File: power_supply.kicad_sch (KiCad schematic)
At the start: 24 parts, among them U3 ST1S10PHR, U4 ST1S09IPUR

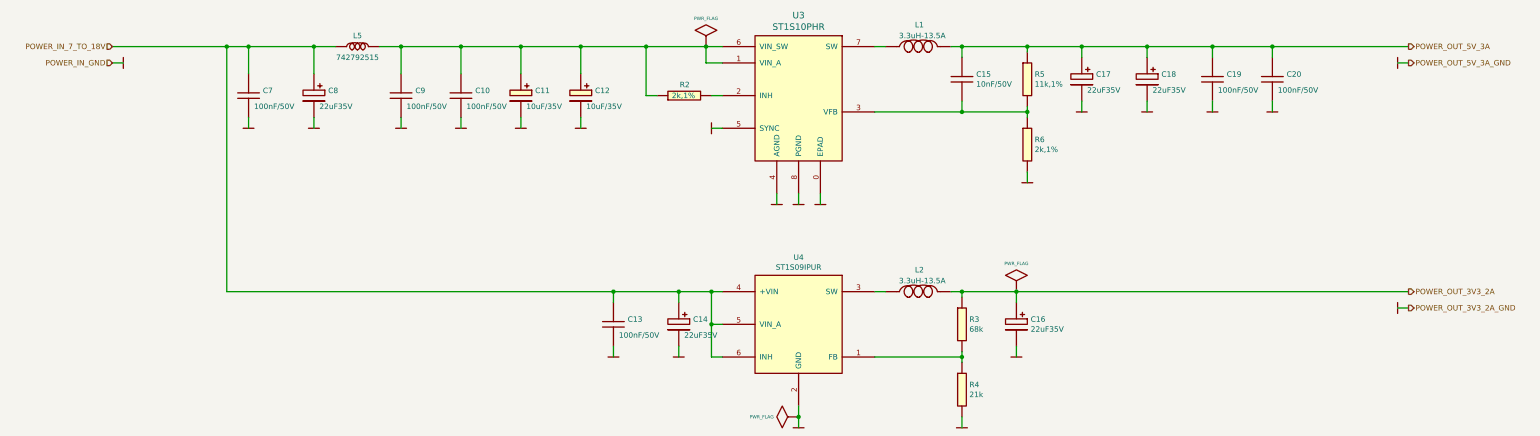
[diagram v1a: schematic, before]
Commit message: Reworked schematic and applied changes on pcb related with mini pci express
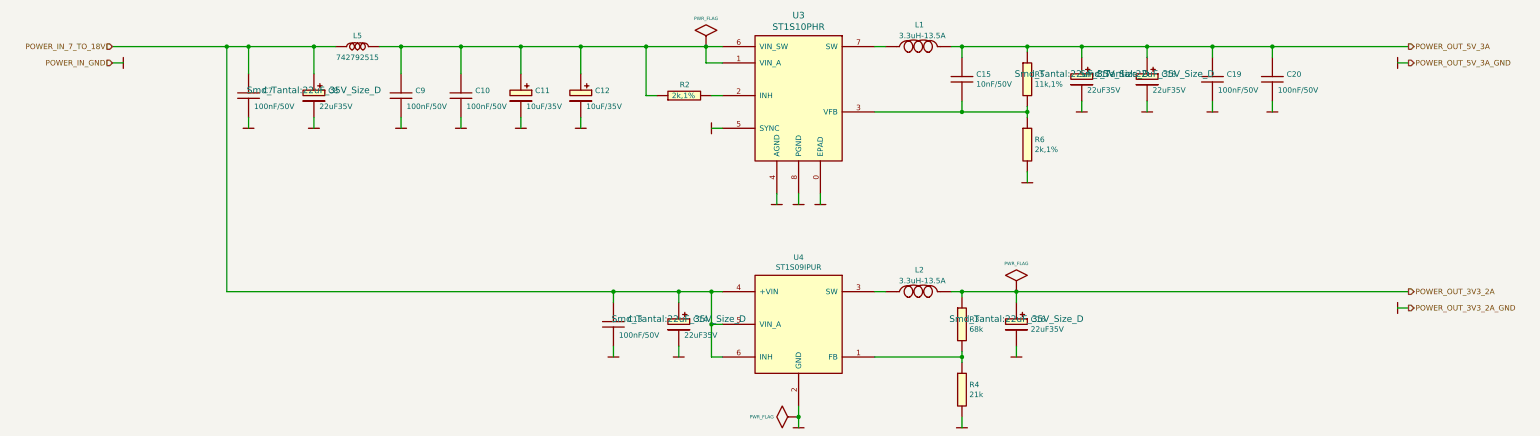
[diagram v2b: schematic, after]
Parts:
- C10, C13, C19, C20, C7, C9: symbol Capacitors_Smd0603:100nF_0603 -> Capacitors_Smd0603:100n
- C14, C16, C17, C18, C8: symbol Capacitors_Smd_Tantal:22uF35V -> Capacitors_Smd_Tantal:22uF_35V
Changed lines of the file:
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@@
     (pin "2")
   )
-  (symbol (lib_id "Capacitors_Smd0603:100nF_0603") (at 85.09 114.3 0) (unit 1)
+  (symbol (lib_id "Capacitors_Smd0603:100n") (at 85.09 114.3 0) (unit 1)
     (in_bom yes) (on_board yes)
     (property "Reference" "C7" (id 0) (at 88.4174 113.1316 0)
@@
     (pin "2")
   )
-  (symbol (lib_id "Capacitors_Smd_Tantal:22uF35V") (at 100.33 113.03 0) (unit 1)
+  (symbol (lib_id "Capacitors_Smd_Tantal:22uF_35V") (at 100.33 113.03 0) (unit 1)
     (in_bom yes) (on_board yes)
     (property "Reference" "C8" (id 0) (at 103.6574 113.1316 0)
@@
     )
     (property "Footprint" "Smd_Tantal:22uF_35V_Size_D" (id 2) (at 100.33 113.03 0)
-      (effects (font (size 1.524 1.524)) hide)
+      (effects (font (size 1.524 1.524)))
     )
     (property "Datasheet" "https://www.tme.eu/Document/a5d90d85079967994fb49c0e8f8ad6e9/293d.pdf" (id 3) (at 100.33 113.03 0)
@@
     (pin "2")
   )
-  (symbol (lib_id "Capacitors_Smd0603:100nF_0603") (at 120.65 114.3 0) (unit 1)
+  (symbol (lib_id "Capacitors_Smd0603:100n") (at 120.65 114.3 0) (unit 1)
     (in_bom yes) (on_board yes)
     (property "Reference" "C9" (id 0) (at 123.9774 113.1316 0)
@@
     (pin "2")
   )
-  (symbol (lib_id "Capacitors_Smd0603:100nF_0603") (at 134.62 114.3 0) (unit 1)
+  (symbol (lib_id "Capacitors_Smd0603:100n") (at 134.62 114.3 0) (unit 1)
     (in_bom yes) (on_board yes)
     (property "Reference" "C10" (id 0) (at 137.9474 113.1316 0)
@@
     (pin "2")
   )
-  (symbol (lib_id "Capacitors_Smd0603:100nF_0603") (at 170.18 167.64 0) (unit 1)
+  (symbol (lib_id "Capacitors_Smd0603:100n") (at 170.18 167.64 0) (unit 1)
     (in_bom yes) (on_board yes)
     (property "Reference" "C13" (id 0) (at 173.5074 166.4716 0)
@@
     (pin "2")
   )
-  (symbol (lib_id "Capacitors_Smd_Tantal:22uF35V") (at 185.42 166.37 0) (unit 1)
+  (symbol (lib_id "Capacitors_Smd_Tantal:22uF_35V") (at 185.42 166.37 0) (unit 1)
     (in_bom yes) (on_board yes)
     (property "Reference" "C14" (id 0) (at 188.7474 166.4716 0)
@@
     )
     (property "Footprint" "Smd_Tantal:22uF_35V_Size_D" (id 2) (at 185.42 166.37 0)
-      (effects (font (size 1.524 1.524)) hide)
+      (effects (font (size 1.524 1.524)))
     )
     (property "Datasheet" "https://www.tme.eu/Document/a5d90d85079967994fb49c0e8f8ad6e9/293d.pdf" (id 3) (at 185.42 166.37 0)
@@
     (pin "2")
   )
-  (symbol (lib_id "Capacitors_Smd_Tantal:22uF35V") (at 264.16 166.37 0) (unit 1)
+  (symbol (lib_id "Capacitors_Smd_Tantal:22uF_35V") (at 264.16 166.37 0) (unit 1)
     (in_bom yes) (on_board yes)
     (property "Reference" "C16" (id 0) (at 267.4874 166.4716 0)
@@
     )
     (property "Footprint" "Smd_Tantal:22uF_35V_Size_D" (id 2) (at 264.16 166.37 0)
-      (effects (font (size 1.524 1.524)) hide)
+      (effects (font (size 1.524 1.524)))
     )
     (property "Datasheet" "https://www.tme.eu/Document/a5d90d85079967994fb49c0e8f8ad6e9/293d.pdf" (id 3) (at 264.16 166.37 0)
@@
     (pin "2")
   )
-  (symbol (lib_id "Capacitors_Smd_Tantal:22uF35V") (at 279.4 109.22 0) (unit 1)
+  (symbol (lib_id "Capacitors_Smd_Tantal:22uF_35V") (at 279.4 109.22 0) (unit 1)
     (in_bom yes) (on_board yes)
     (property "Reference" "C17" (id 0) (at 282.7274 109.3216 0)
@@
     )
     (property "Footprint" "Smd_Tantal:22uF_35V_Size_D" (id 2) (at 279.4 109.22 0)
-      (effects (font (size 1.524 1.524)) hide)
+      (effects (font (size 1.524 1.524)))
     )
     (property "Datasheet" "https://www.tme.eu/Document/a5d90d85079967994fb49c0e8f8ad6e9/293d.pdf" (id 3) (at 279.4 109.22 0)
@@
     (pin "2")
   )
-  (symbol (lib_id "Capacitors_Smd_Tantal:22uF35V") (at 294.64 109.22 0) (unit 1)
+  (symbol (lib_id "Capacitors_Smd_Tantal:22uF_35V") (at 294.64 109.22 0) (unit 1)
     (in_bom yes) (on_board yes)
     (property "Reference" "C18" (id 0) (at 297.9674 109.3216 0)
@@
     )
     (property "Footprint" "Smd_Tantal:22uF_35V_Size_D" (id 2) (at 294.64 109.22 0)
-      (effects (font (size 1.524 1.524)) hide)
+      (effects (font (size 1.524 1.524)))
     )
     (property "Datasheet" "https://www.tme.eu/Document/a5d90d85079967994fb49c0e8f8ad6e9/293d.pdf" (id 3) (at 294.64 109.22 0)
@@
     (pin "2")
   )
-  (symbol (lib_id "Capacitors_Smd0603:100nF_0603") (at 309.88 110.49 0) (unit 1)
+  (symbol (lib_id "Capacitors_Smd0603:100n") (at 309.88 110.49 0) (unit 1)
     (in_bom yes) (on_board yes)
     (property "Reference" "C19" (id 0) (at 313.2074 109.3216 0)
@@
     (pin "2")
   )
-  (symbol (lib_id "Capacitors_Smd0603:100nF_0603") (at 323.85 110.49 0) (unit 1)
+  (symbol (lib_id "Capacitors_Smd0603:100n") (at 323.85 110.49 0) (unit 1)
     (in_bom yes) (on_board yes)
     (property "Reference" "C20" (id 0) (at 327.1774 109.3216 0)
